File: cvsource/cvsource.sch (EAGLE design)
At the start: 101 parts, among them IC1 OPA4130P, IC2 OPA2134P, IC3 78L05Z, J1 UBBS-4R-D14-4D, P1 US-EVUF3J, P2 US-EVUF3J, P3 US-EVUF3J, P4 US-EVUF3J, X1 2516-

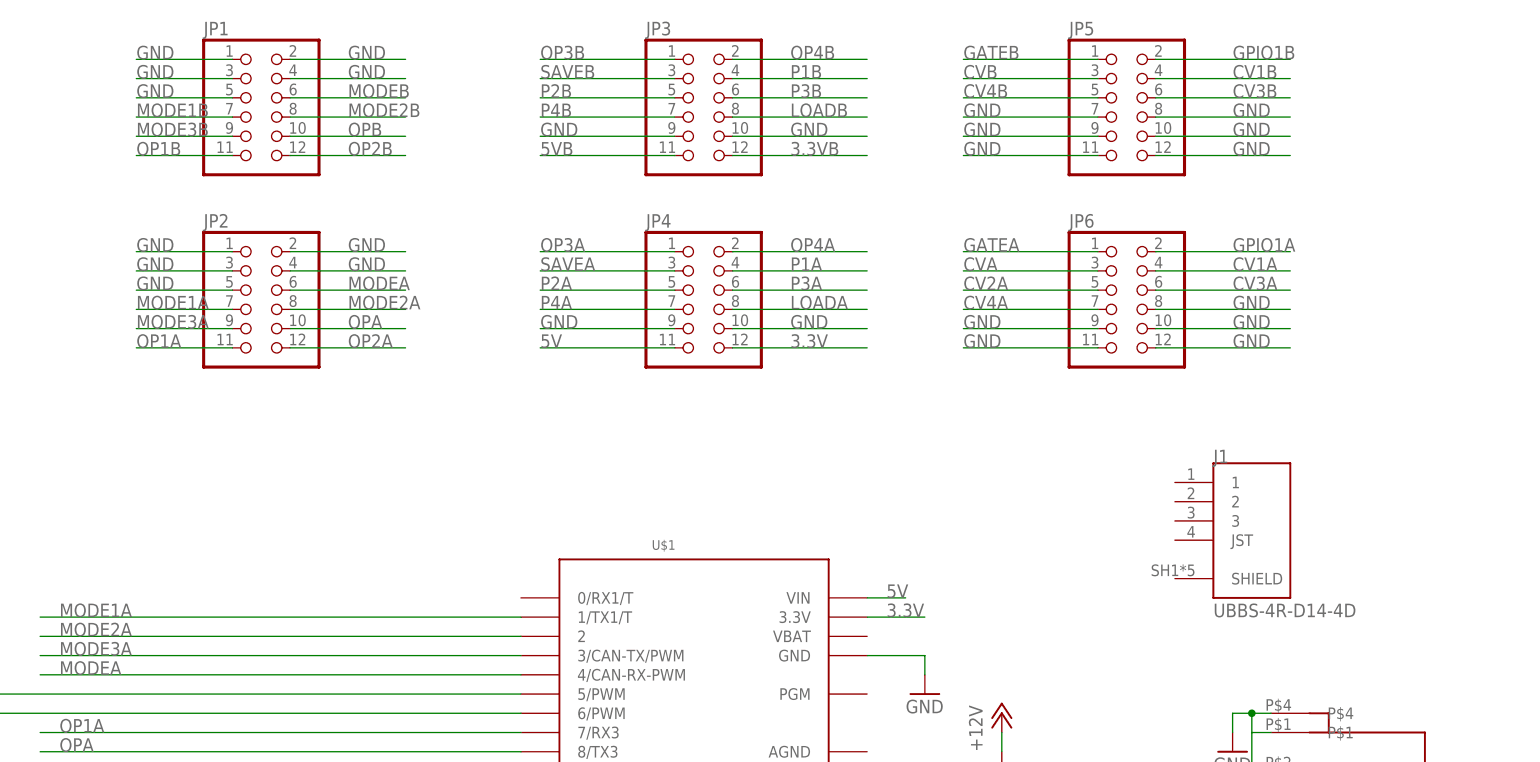
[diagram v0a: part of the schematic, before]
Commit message: added usb and moved things on cvsource
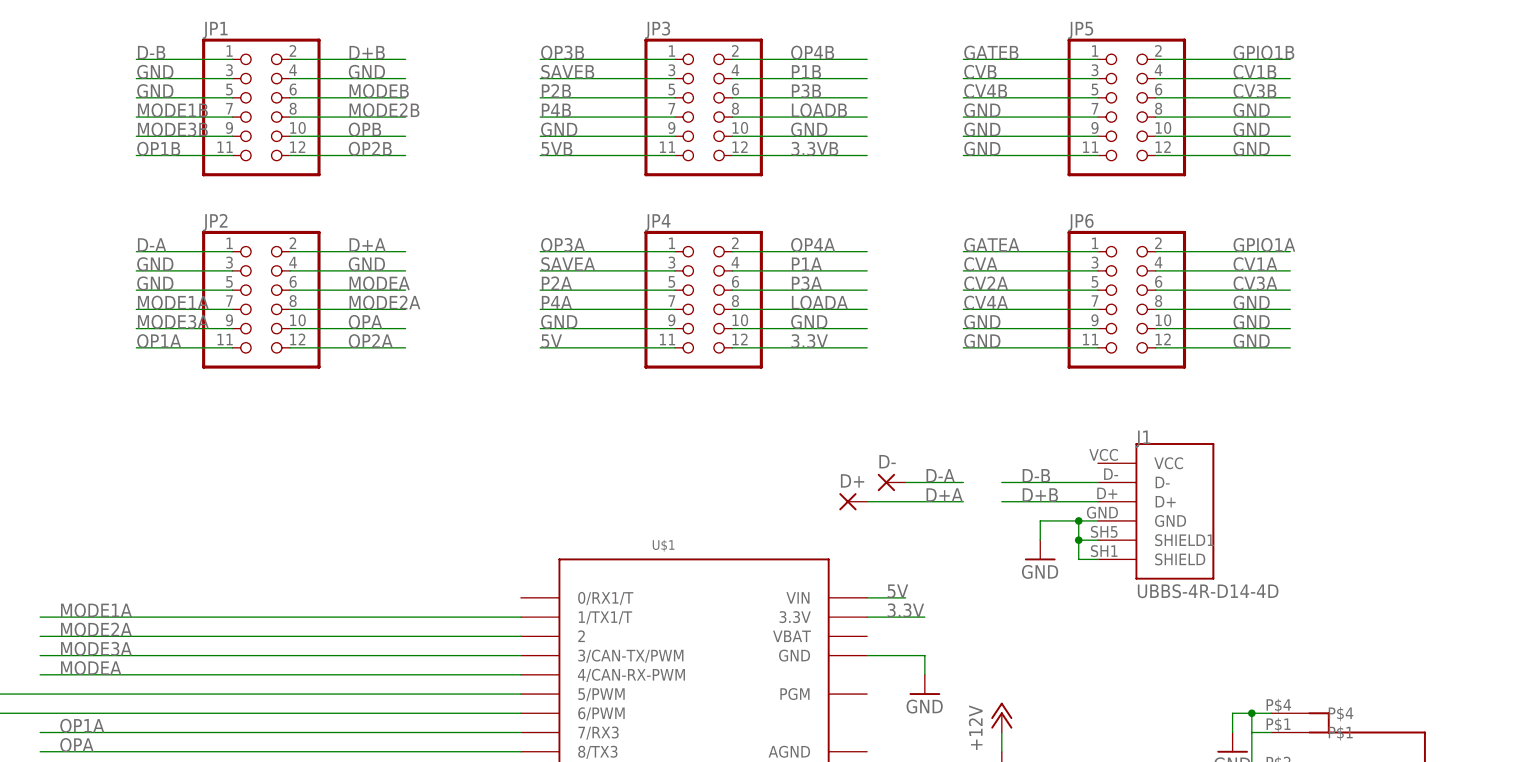
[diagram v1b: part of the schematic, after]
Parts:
- added D+, D-: (no value), synthdiy:2,0/0,9-R
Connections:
- new net D+A: D+.P, JP2.2
- new net D+B: J1.D+, JP1.2
- new net D-A: D-.P, JP2.1
- new net D-B: J1.D-, JP1.1
- net GND: now also J1.GND, J1.SHIELD, J1.SHIELD1; no longer JP1.1, JP1.2, JP2.1, JP2.2
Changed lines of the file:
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@@
 <part name="JP6" library="dan" deviceset="PINHD-2X6" device=""/>
 <part name="CVOUT6" library="dan" deviceset="PJ301BM" device=""/>
-<part name="J1" library="UBBS-4R-D14-4D" deviceset="UBBS-4R-D14-4D" device=""/>
 <part name="CVOUT7" library="dan" deviceset="PJ301BM" device=""/>
 <part name="GND40" library="dan" deviceset="GND" device=""/>
 <part name="R38" library="dan" deviceset="R-US_" device="0207/2V" value="1k"/>
+<part name="D-" library="synthdiy" deviceset="2,0/0,9-R" device=""/>
+<part name="D+" library="synthdiy" deviceset="2,0/0,9-R" device=""/>
+<part name="J1" library="UBBS-4R-D14-4D" deviceset="UBBS-4R-D14-4D" device=""/>
+<part name="GND41" library="dan" deviceset="GND" device=""/>
 </parts>
 <sheets>
@@
 <instance part="JP6" gate="A" x="111.76" y="119.38"/>
 <instance part="CVOUT6" gate="G$1" x="142.24" y="40.64" rot="MR0"/>
-<instance part="J1" gate="G$1" x="129.54" y="88.9"/>
 <instance part="CVOUT7" gate="G$1" x="91.44" y="-10.16" rot="MR0"/>
 <instance part="GND40" gate="1" x="76.2" y="-7.62"/>
 <instance part="R38" gate="G$1" x="63.5" y="-15.24" rot="R180"/>
+<instance part="D-" gate="P" x="81.28" y="93.98"/>
+<instance part="D+" gate="P" x="76.2" y="91.44"/>
+<instance part="J1" gate="G$1" x="119.38" y="91.44"/>
+<instance part="GND41" gate="1" x="101.6" y="83.82"/>
 </instances>
 <busses>
@@
 </segment>
 <segment>
-<pinref part="JP2" gate="A" pin="1"/>
-<wire x1="-5.08" y1="124.46" x2="-17.78" y2="124.46" width="0.1524" layer="91"/>
-<label x="-17.78" y="124.46" size="1.778" layer="95"/>
-</segment>
-<segment>
-<pinref part="JP2" gate="A" pin="2"/>
-<wire x1="2.54" y1="124.46" x2="17.78" y2="124.46" width="0.1524" layer="91"/>
-<label x="10.16" y="124.46" size="1.778" layer="95"/>
-</segment>
-<segment>
 <pinref part="JP2" gate="A" pin="3"/>
 <wire x1="-5.08" y1="121.92" x2="-17.78" y2="121.92" width="0.1524" layer="91"/>
@@
 </segment>
 <segment>
-<pinref part="JP1" gate="A" pin="1"/>
-<wire x1="-5.08" y1="149.86" x2="-17.78" y2="149.86" width="0.1524" layer="91"/>
-<label x="-17.78" y="149.86" size="1.778" layer="95"/>
-</segment>
-<segment>
-<pinref part="JP1" gate="A" pin="2"/>
-<wire x1="2.54" y1="149.86" x2="17.78" y2="149.86" width="0.1524" layer="91"/>
-<label x="10.16" y="149.86" size="1.778" layer="95"/>
-</segment>
-<segment>
 <pinref part="JP1" gate="A" pin="3"/>
 <wire x1="-5.08" y1="147.32" x2="-17.78" y2="147.32" width="0.1524" layer="91"/>
@@
 <pinref part="GND20" gate="1" pin="GND"/>
 <wire x1="-195.58" y1="-93.98" x2="-195.58" y2="-96.52" width="0.1524" layer="91"/>
+</segment>
+<segment>
+<pinref part="GND41" gate="1" pin="GND"/>
+<wire x1="101.6" y1="86.36" x2="101.6" y2="88.9" width="0.1524" layer="91"/>
+<pinref part="J1" gate="G$1" pin="SHIELD"/>
+<wire x1="109.22" y1="83.82" x2="106.68" y2="83.82" width="0.1524" layer="91"/>
+<wire x1="106.68" y1="83.82" x2="106.68" y2="86.36" width="0.1524" layer="91"/>
+<pinref part="J1" gate="G$1" pin="GND"/>
+<wire x1="106.68" y1="86.36" x2="106.68" y2="88.9" width="0.1524" layer="91"/>
+<wire x1="106.68" y1="88.9" x2="109.22" y2="88.9" width="0.1524" layer="91"/>
+<pinref part="J1" gate="G$1" pin="SHIELD1"/>
+<wire x1="109.22" y1="86.36" x2="106.68" y2="86.36" width="0.1524" layer="91"/>
+<junction x="106.68" y="86.36"/>
+<wire x1="101.6" y1="88.9" x2="106.68" y2="88.9" width="0.1524" layer="91"/>
+<junction x="106.68" y="88.9"/>
 </segment>
 </net>
@@
 </segment>
 </net>
+<net name="D-A" class="0">
+<segment>
+<pinref part="JP2" gate="A" pin="1"/>
+<wire x1="-5.08" y1="124.46" x2="-17.78" y2="124.46" width="0.1524" layer="91"/>
+<label x="-17.78" y="124.46" size="1.778" layer="95"/>
+</segment>
+<segment>
+<pinref part="D-" gate="P" pin="P"/>
+<wire x1="83.82" y1="93.98" x2="91.44" y2="93.98" width="0.1524" layer="91"/>
+<label x="86.36" y="93.98" size="1.778" layer="95"/>
+</segment>
+</net>
+<net name="D+A" class="0">
+<segment>
+<pinref part="JP2" gate="A" pin="2"/>
+<wire x1="2.54" y1="124.46" x2="17.78" y2="124.46" width="0.1524" layer="91"/>
+<label x="10.16" y="124.46" size="1.778" layer="95"/>
+</segment>
+<segment>
+<pinref part="D+" gate="P" pin="P"/>
+<wire x1="78.74" y1="91.44" x2="91.44" y2="91.44" width="0.1524" layer="91"/>
+<label x="86.36" y="91.44" size="1.778" layer="95"/>
+</segment>
+</net>
+<net name="D+B" class="0">
+<segment>
+<pinref part="JP1" gate="A" pin="2"/>
+<wire x1="2.54" y1="149.86" x2="17.78" y2="149.86" width="0.1524" layer="91"/>
+<label x="10.16" y="149.86" size="1.778" layer="95"/>
+</segment>
+<segment>
+<pinref part="J1" gate="G$1" pin="D+"/>
+<wire x1="109.22" y1="91.44" x2="96.52" y2="91.44" width="0.1524" layer="91"/>
+<label x="99.06" y="91.44" size="1.778" layer="95"/>
+</segment>
+</net>
+<net name="D-B" class="0">
+<segment>
+<pinref part="JP1" gate="A" pin="1"/>
+<wire x1="-5.08" y1="149.86" x2="-17.78" y2="149.86" width="0.1524" layer="91"/>
+<label x="-17.78" y="149.86" size="1.778" layer="95"/>
+</segment>
+<segment>
+<pinref part="J1" gate="G$1" pin="D-"/>
+<wire x1="109.22" y1="93.98" x2="96.52" y2="93.98" width="0.1524" layer="91"/>
+<label x="99.06" y="93.98" size="1.778" layer="95"/>
+</segment>
+</net>

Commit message: moved things around on cvsource
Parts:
- added GATE: (no value), dan:LED5MM
- added R39: 10k, dan:R-US_0207/2V
- renumbered J1 to USB
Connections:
- new net N$6: GATE.C, R39.2
- net GATEB: now also GATE.A
- net GND: now also R39.1
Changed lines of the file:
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@@
 <part name="D-" library="synthdiy" deviceset="2,0/0,9-R" device=""/>
 <part name="D+" library="synthdiy" deviceset="2,0/0,9-R" device=""/>
-<part name="J1" library="UBBS-4R-D14-4D" deviceset="UBBS-4R-D14-4D" device=""/>
+<part name="USB" library="UBBS-4R-D14-4D" deviceset="UBBS-4R-D14-4D" device=""/>
 <part name="GND41" library="dan" deviceset="GND" device=""/>
+<part name="GATE" library="dan" deviceset="LED" device="5MM"/>
+<part name="R39" library="dan" deviceset="R-US_" device="0207/2V" value="10k"/>
+<part name="GND42" library="dan" deviceset="GND" device=""/>
 </parts>
 <sheets>
@@
 <instance part="D-" gate="P" x="81.28" y="93.98"/>
 <instance part="D+" gate="P" x="76.2" y="91.44"/>
-<instance part="J1" gate="G$1" x="119.38" y="91.44"/>
+<instance part="USB" gate="G$1" x="119.38" y="91.44"/>
 <instance part="GND41" gate="1" x="101.6" y="83.82"/>
+<instance part="GATE" gate="G$1" x="177.8" y="10.16"/>
+<instance part="R39" gate="G$1" x="177.8" y="-2.54" rot="R90"/>
+<instance part="GND42" gate="1" x="177.8" y="-12.7"/>
 </instances>
 <busses>
@@
 <pinref part="GND41" gate="1" pin="GND"/>
 <wire x1="101.6" y1="86.36" x2="101.6" y2="88.9" width="0.1524" layer="91"/>
-<pinref part="J1" gate="G$1" pin="SHIELD"/>
+<pinref part="USB" gate="G$1" pin="SHIELD"/>
 <wire x1="109.22" y1="83.82" x2="106.68" y2="83.82" width="0.1524" layer="91"/>
 <wire x1="106.68" y1="83.82" x2="106.68" y2="86.36" width="0.1524" layer="91"/>
-<pinref part="J1" gate="G$1" pin="GND"/>
+<pinref part="USB" gate="G$1" pin="GND"/>
 <wire x1="106.68" y1="86.36" x2="106.68" y2="88.9" width="0.1524" layer="91"/>
 <wire x1="106.68" y1="88.9" x2="109.22" y2="88.9" width="0.1524" layer="91"/>
-<pinref part="J1" gate="G$1" pin="SHIELD1"/>
+<pinref part="USB" gate="G$1" pin="SHIELD1"/>
 <wire x1="109.22" y1="86.36" x2="106.68" y2="86.36" width="0.1524" layer="91"/>
 <junction x="106.68" y="86.36"/>
 <wire x1="101.6" y1="88.9" x2="106.68" y2="88.9" width="0.1524" layer="91"/>
 <junction x="106.68" y="88.9"/>
+</segment>
+<segment>
+<pinref part="R39" gate="G$1" pin="1"/>
+<pinref part="GND42" gate="1" pin="GND"/>
+<wire x1="177.8" y1="-10.16" x2="177.8" y2="-7.62" width="0.1524" layer="91"/>
 </segment>
 </net>
@@
 <segment>
 <pinref part="CVOUT5" gate="G$1" pin="P$3"/>
-<wire x1="175.26" y1="17.78" x2="162.56" y2="17.78" width="0.1524" layer="91"/>
+<wire x1="175.26" y1="17.78" x2="172.72" y2="17.78" width="0.1524" layer="91"/>
 <label x="165.1" y="17.78" size="1.778" layer="95"/>
+<pinref part="GATE" gate="G$1" pin="A"/>
+<wire x1="172.72" y1="17.78" x2="162.56" y2="17.78" width="0.1524" layer="91"/>
+<wire x1="177.8" y1="12.7" x2="172.72" y2="12.7" width="0.1524" layer="91"/>
+<wire x1="172.72" y1="12.7" x2="172.72" y2="17.78" width="0.1524" layer="91"/>
 </segment>
 <segment>
@@
 </segment>
 <segment>
-<pinref part="J1" gate="G$1" pin="D+"/>
+<pinref part="USB" gate="G$1" pin="D+"/>
 <wire x1="109.22" y1="91.44" x2="96.52" y2="91.44" width="0.1524" layer="91"/>
 <label x="99.06" y="91.44" size="1.778" layer="95"/>
@@
 </segment>
 <segment>
-<pinref part="J1" gate="G$1" pin="D-"/>
+<pinref part="USB" gate="G$1" pin="D-"/>
 <wire x1="109.22" y1="93.98" x2="96.52" y2="93.98" width="0.1524" layer="91"/>
 <label x="99.06" y="93.98" size="1.778" layer="95"/>
 </segment>
 </net>
+<net name="N$6" class="0">
+<segment>
+<pinref part="R39" gate="G$1" pin="2"/>
+<pinref part="GATE" gate="G$1" pin="C"/>
+<wire x1="177.8" y1="2.54" x2="177.8" y2="5.08" width="0.1524" layer="91"/>
+</segment>
+</net>
